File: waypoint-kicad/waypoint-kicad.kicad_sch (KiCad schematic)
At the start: 73 parts, among them J1 USB_C_Receptacle_USB2.0_14P, J2 Conn_01x02, J3 Conn_Coaxial, J4 Conn_02x03_Odd_Even, J5 Conn_01x08, J6 Conn_01x02, Q1 NPN, SW1 SW_SPST, U1 nRF52840, U2 SX1262IMLTRT, U3 AP2112K-3.3, U4 MCP73831-2-OT, U5 DRV2605LDGS, U6 LIS2DH, Y1 Crystal_GND24, Y2 Crystal, Y3 XO32

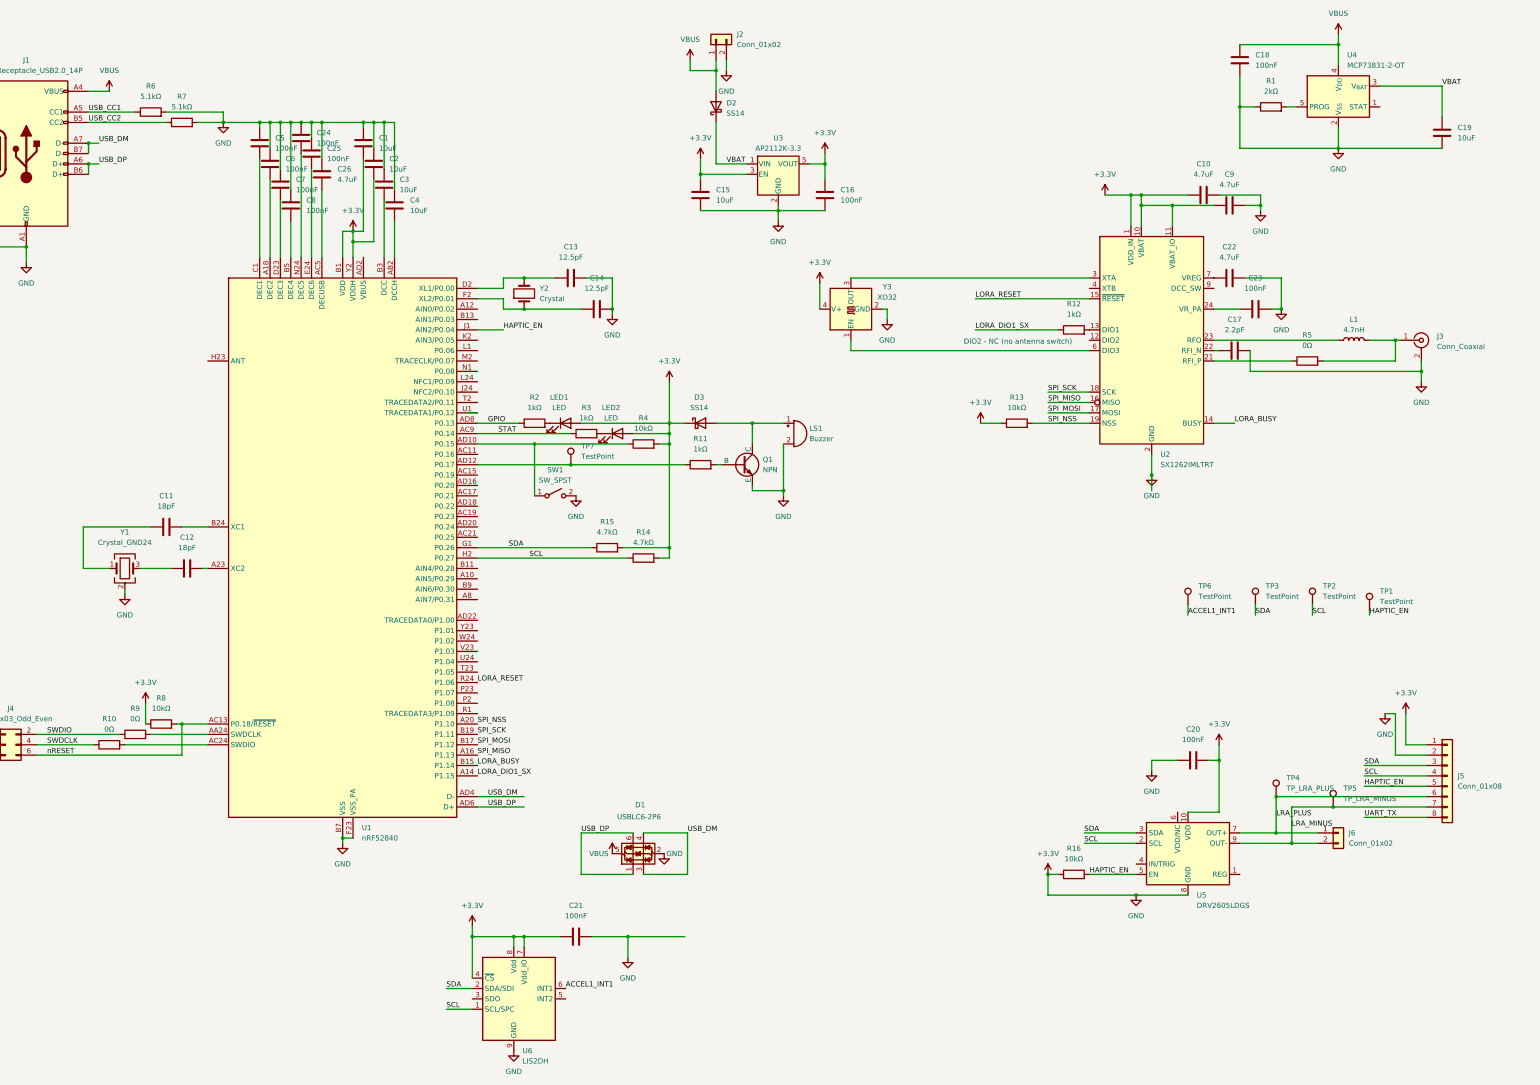
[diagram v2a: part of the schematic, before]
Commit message: Enhance waypoint-kicad documentation and component definitions
- Added battery voltage monitoring section with detailed pin assignments and ADC calculations.
- Updated pin assignments for U1-U6 ICs, including new connections for the antenna and TCXO.
- Revised capacitor and diode components with updated values, footprints, and datasheets.
- Removed obsolete fixed connections and netlist files to streamline project structure.
- Introduced new components for improved design clarity and accuracy.
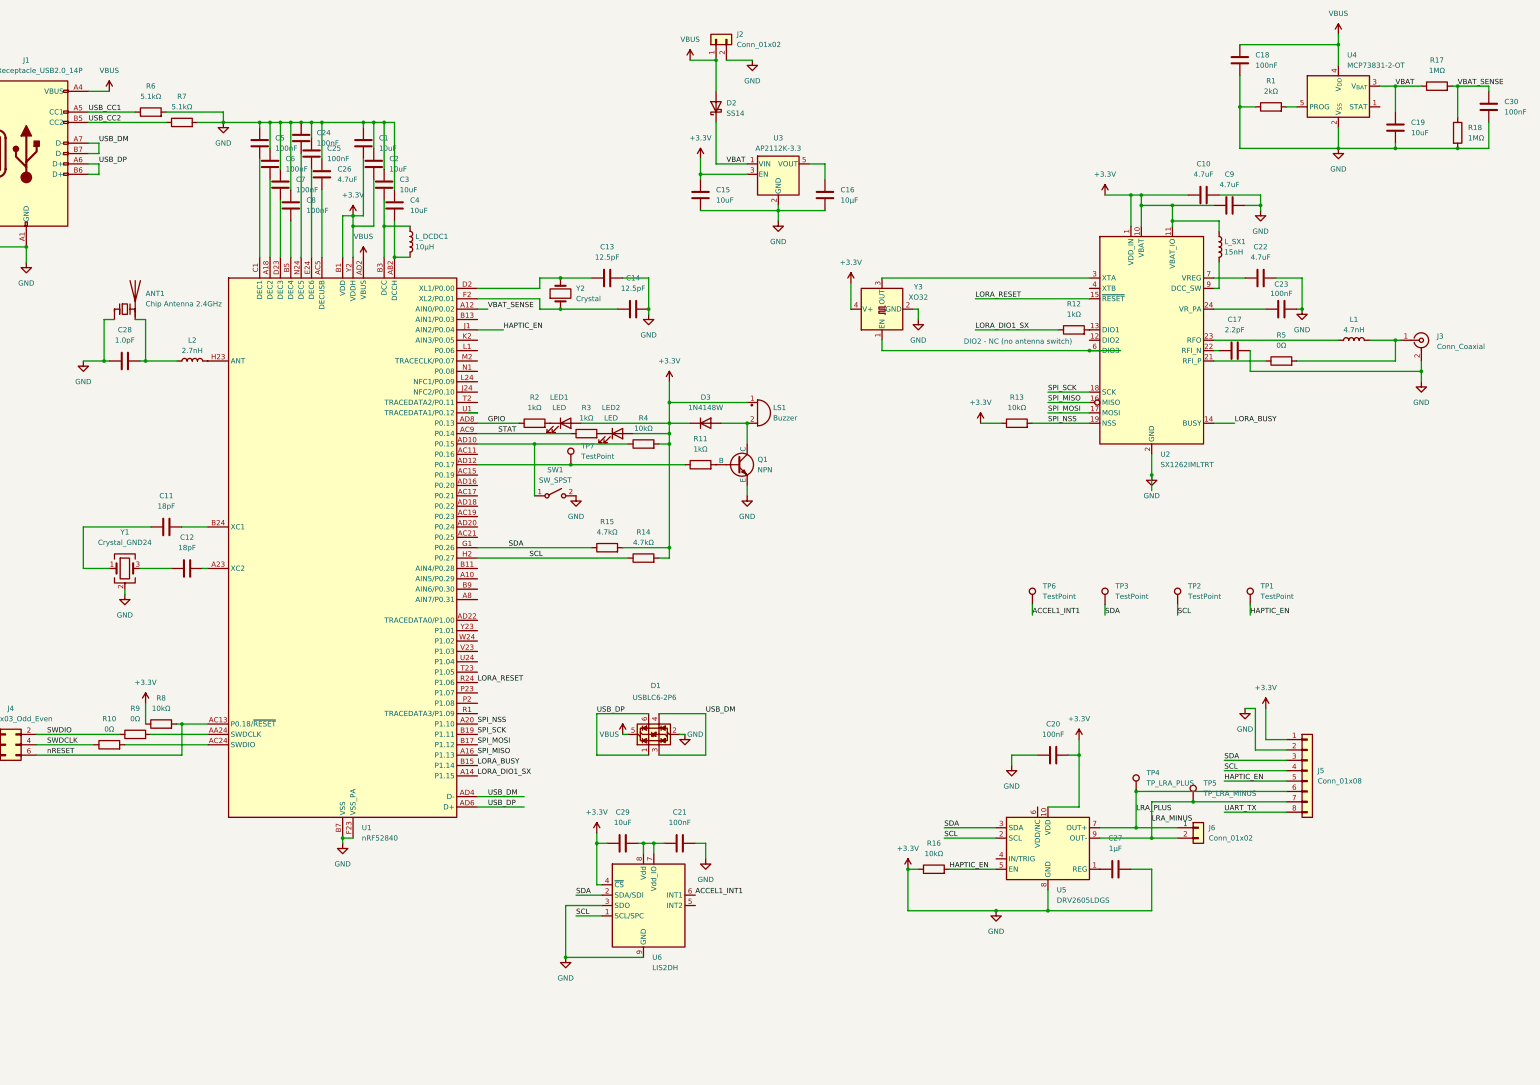
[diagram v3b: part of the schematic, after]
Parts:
- removed D3: SS14, Diode_SMD:D_SMA, symbol Diode:SS14
- added ANT1: Chip Antenna 2.4GHz, Capacitor_SMD:C_1206_3216Metric_Pad1.33x1.80mm_HandSolder, symbol Device:Antenna_Chip
- added C27: 1µF, Capacitor_SMD:C_0402_1005Metric_Pad0.74x0.62mm_HandSolder, symbol Device:C
- added C28: 1.0pF, Capacitor_SMD:C_0402_1005Metric_Pad0.74x0.62mm_HandSolder, symbol Device:C
- added C29: 10uF, Capacitor_SMD:C_0805_2012Metric_Pad1.18x1.45mm_HandSolder, symbol Device:C
- added C30: 100nF, Capacitor_SMD:C_0402_1005Metric_Pad0.74x0.62mm_HandSolder, symbol Device:C
- added D3: 1N4148W, Diode_SMD:D_SOD-123, symbol Diode:1N4148W
- added L2: 2.7nH, Inductor_SMD:L_0402_1005Metric_Pad0.77x0.64mm_HandSolder, symbol Device:L
- added L_DCDC1: 10µH, Inductor_SMD:L_0805_2012Metric_Pad1.05x1.20mm_HandSolder, symbol Device:L
- added L_SX1: 15nH, Inductor_SMD:L_0402_1005Metric_Pad0.77x0.64mm_HandSolder, symbol Device:L
- added R17, R18: 1MΩ, Resistor_SMD:R_0402_1005Metric_Pad0.72x0.64mm_HandSolder, symbol Device:R
- C16: value 100nF -> 10µF
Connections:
- net +3.3V: now also LS1.1 (+), U6.3 (SDO), ANT1.1 (FEED), C27.1, C28.1, C29.1, C30.1, D3.1 (K), L_SX1.1, R18.2; no longer C16.2, C21.1, LS1.2 (-), U3.5 (VOUT), U6.7 (Vdd_IO), U6.8 (Vdd)
- net VBAT: now also R17.1
- net VBUS: now also U1.AD2 (VBUS)
- net at Q1.1 (C): now also LS1.2 (-), D3.2 (A); no longer LS1.1 (+)
- net at C3.2, U1.B3 (DCC): now also L_DCDC1.1
- net at U2.9 (DCC_SW): now also L_SX1.2
- net at U5.1 (REG): now also C27.2
- net at C4.2, U1.AB2 (DCCH): now also L_DCDC1.2
- net VBAT_SENSE: now reaches U1.A12 (AIN0/P0.02)
- net VBAT_SENSE: now also C30.2, R17.2, R18.1
- net at U1.H23 (ANT): now also L2.2
- new net: ANT1.2 (PCB_Trace), C28.2, L2.1
- new net: C21.1, C29.2, U6.7 (Vdd_IO), U6.8 (Vdd)
- new net: C16.2, U3.5 (VOUT)
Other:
- moved on the sheet: C13, C14, C19, C20, C21, C22, C23, D1, J5, J6, LS1, Q1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
